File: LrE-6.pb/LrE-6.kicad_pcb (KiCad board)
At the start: 2 copper layers, 100 x 100 mm, 110 parts, among them J1 USB_B_Micro, J2 SM06B-SRSS-TB, Q1 2N7002, SW1 SW_Push_45deg, SW10 SW_Push_45deg, SW11 Rotary_Encoder_Switch, SW12 Rotary_Encoder_Switch, SW13 Rotary_Encoder_Switch, SW14 Rotary_Encoder_Switch, SW15 Rotary_Encoder_Switch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

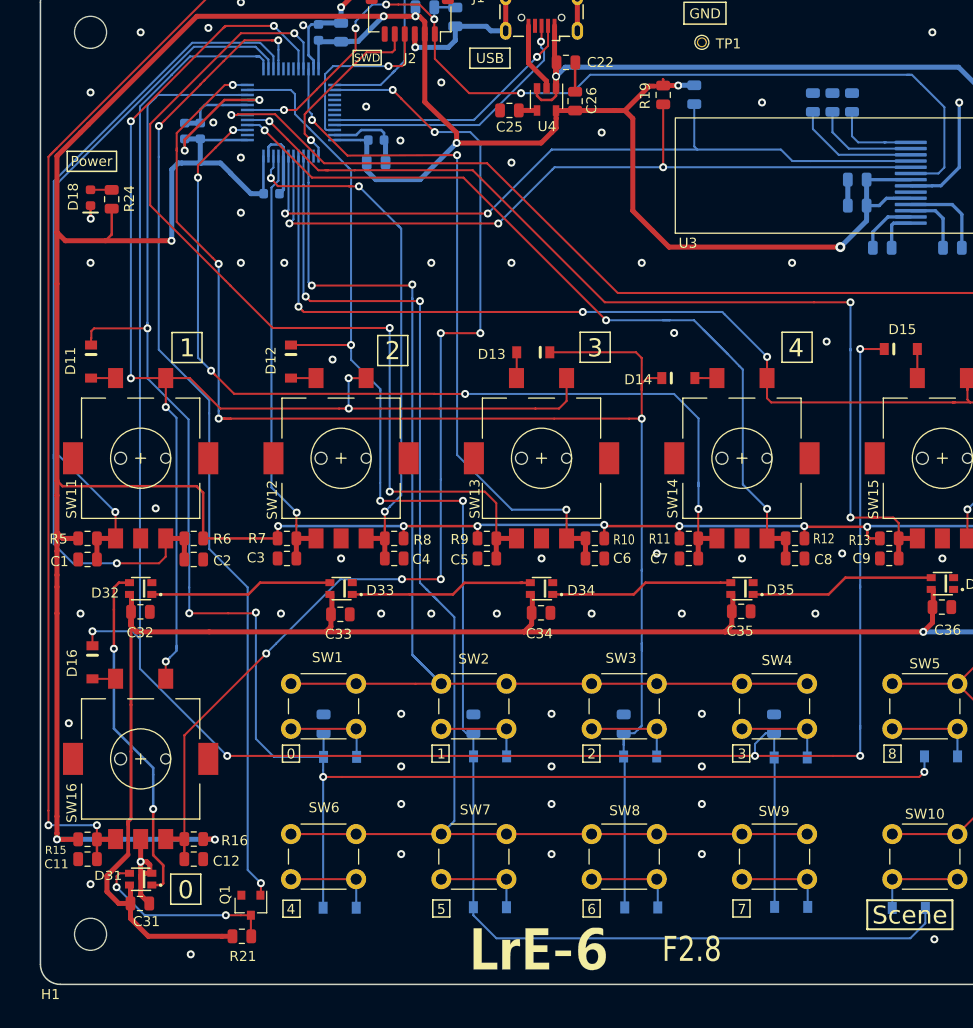
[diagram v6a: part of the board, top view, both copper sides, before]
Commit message: 0.37-6
Fix pb for OLED stability.
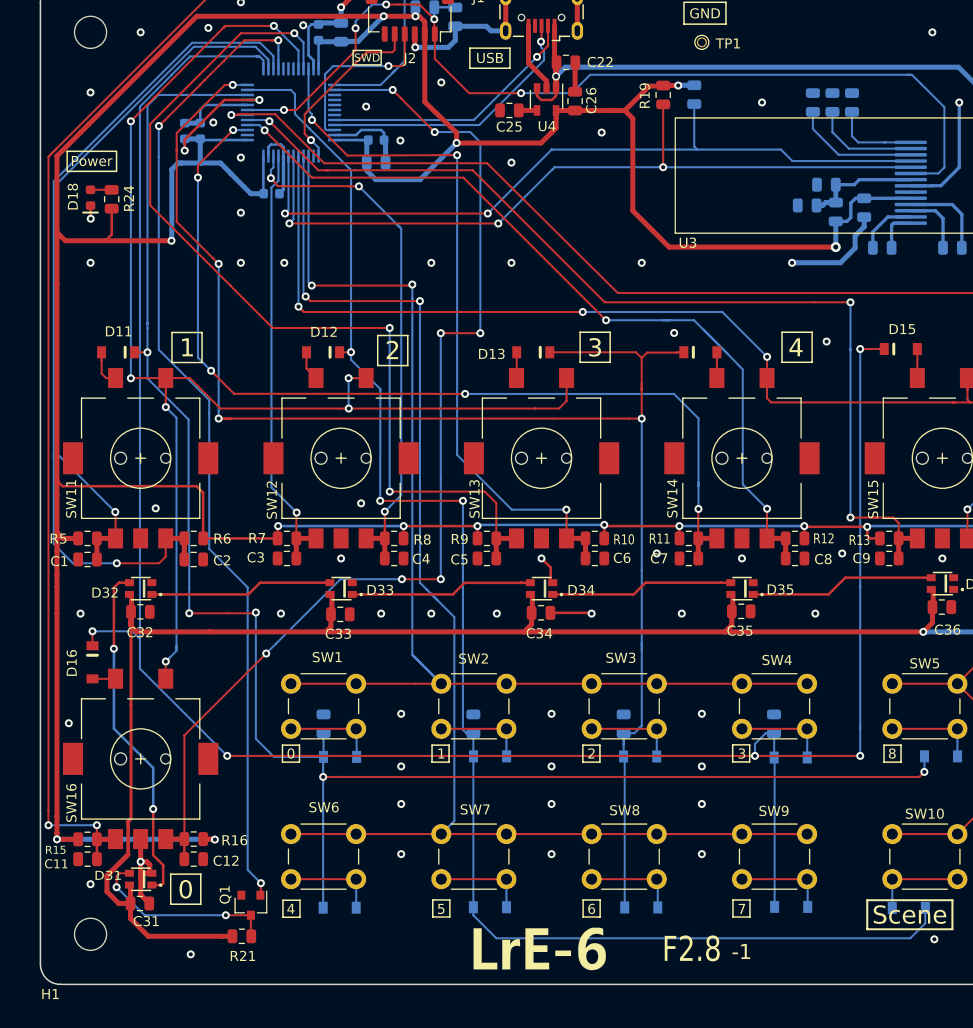
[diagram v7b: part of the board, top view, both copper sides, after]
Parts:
- added R22: 1K, Resistor_SMD:R_0805_2012Metric, B.Cu at (176.5, 122.3)
- added R23: 100, Resistor_SMD:R_0805_2012Metric, B.Cu at (179.4, 122.9)
- C15, C19: value 10u -> 4.7u
- C28, C29: value 2.2u -> 4.7u
- D18: value LED GR -> LED0603_BL
- D31, D32, D33, D34, D35, D36: value WS2812B -> WS2812B-2020
- R18: value 390K -> 62
- R21: value 4.7K -> 10K
- R24: value 470 -> 1K
- SW1, SW10, SW2, SW3, SW4, SW5, SW6, SW7, SW8, SW9: value SW_Push_45deg -> Tact_SW_8mm
- SW11, SW12, SW13, SW14, SW15, SW16: value Rotary_Encoder_Switch -> EC11_SMD
- U3: value OLED-0.91 -> SSD1306_OLED_0.91
- moved ? 3.39 mm to (165.8, 136.9)
- moved D12 3.33 mm to (128.2, 136.9), turned to 180 degrees
- moved C27 3.12 mm to (178.4, 120.2)
- moved D11 2.85 mm to (107.8, 136.9), turned to 180 degrees
- moved C20 0.73 mm to (182.2, 122.5), turned to 270 degrees
- renumbered D14 to ?
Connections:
- C27 pad 2: +3V3 -> Net-(C27-Pad2)
- U3 pad 8: +3V3 -> Net-(C27-Pad2)
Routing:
- net GND: track 112.0 -> 126.7 mm
- net Net-(C27-Pad2): track 0.00 -> 11.5 mm
- net +3V3: track 421.1 -> 414.9 mm
- net /M0: track 177.4 -> 171.6 mm
- net /M1: track 154.3 -> 149.5 mm
- net /M2: track 153.8 -> 156.0 mm
- net Net-(D11-Pad2): track 2.45 -> 3.71 mm
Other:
- board text added: "-1"
